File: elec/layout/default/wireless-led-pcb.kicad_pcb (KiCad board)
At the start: 4 copper layers, 154 x 30 mm, 47 parts

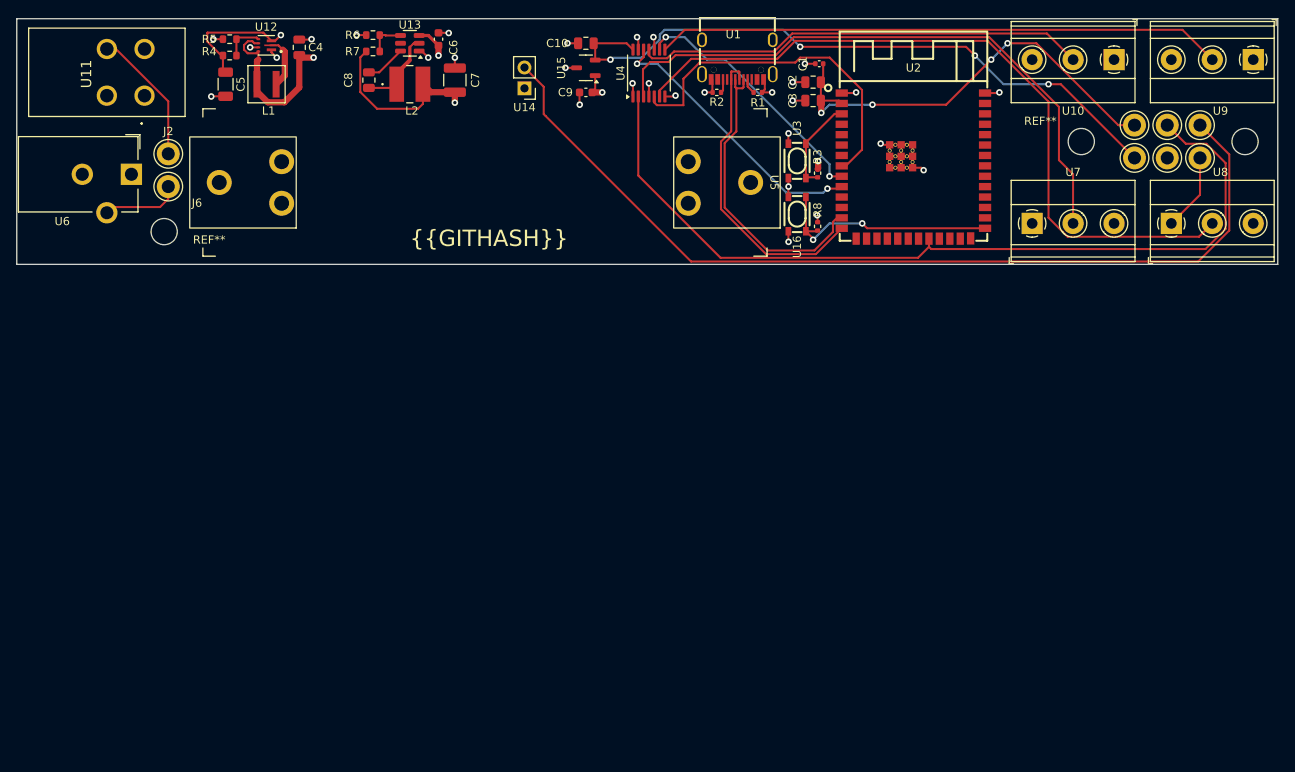
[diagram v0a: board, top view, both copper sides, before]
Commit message: totally new layout, much smaller, tons of pours.
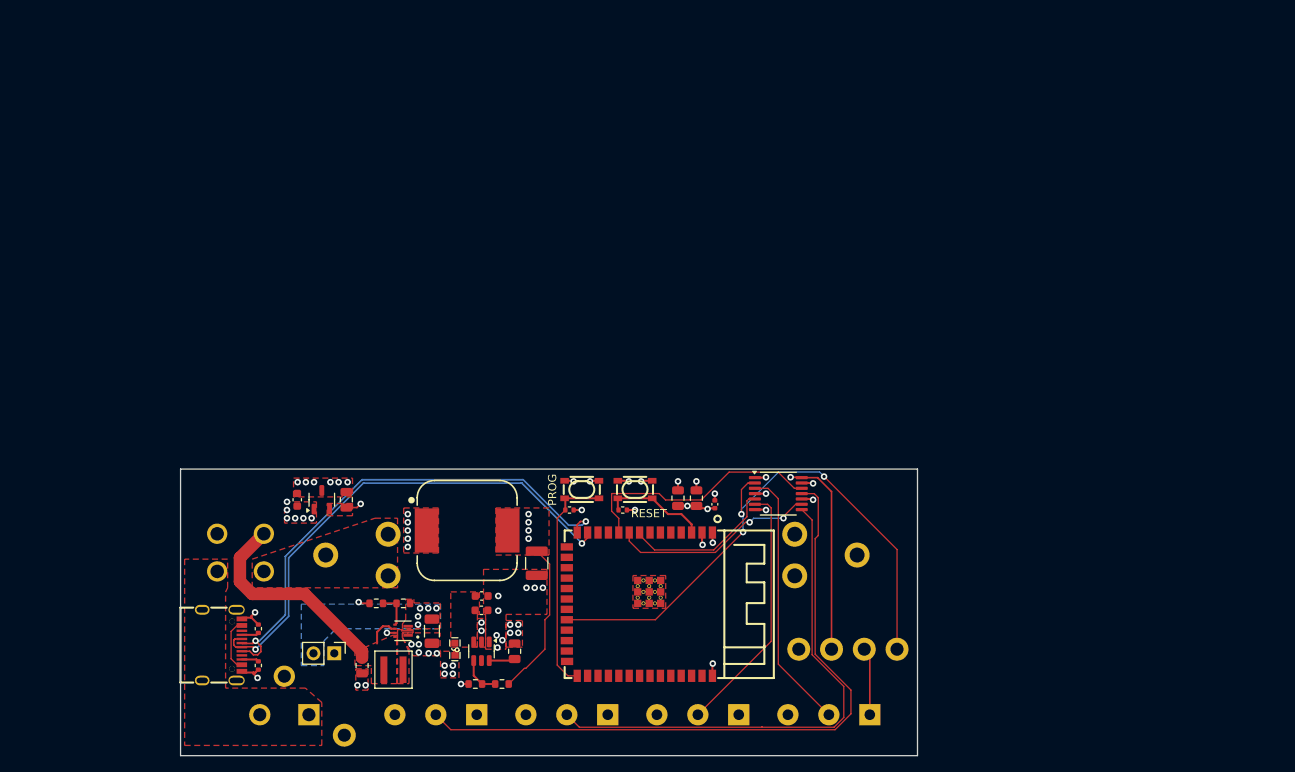
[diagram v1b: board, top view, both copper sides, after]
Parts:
- removed the J2 at (48.5, 86.5)
- removed J7, J8: , TestPoint:TestPoint_Keystone_5005-5009_Compact
- removed REF** (x3): MountingHole_3.2mm_M3, MountingHole:MountingHole_3.2mm_M3
- added C7: 50V 100nF X7R ±10% 0603 Multilayer Ceramic Capacitors MLCC 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, lib:C0603, F.Cu at (86.8, 140.5)
- added U14: , lib:F0603, F.Cu at (83.5, 147.0)
- C6: value 10V 3.3uF X5R ±10% 0603 Multilayer Ceramic Capacitors MLCC - SMD/SMT ROHS -> 25V 3.3uF X5R ±10% 0603 Multilayer Ceramic Capacitors MLCC - SMD/SMT ROHS
- J1, U10, U11, U5, U6, U7, U8, U9: moved to B.Cu
- J2: renamed from J3; moved to B.Cu
- J3: renamed from J4; moved to B.Cu
- J4: renamed from J5; moved to B.Cu
- J5: renamed from J6; moved to B.Cu
- L2: value 6.8uH +/- 20% -> 10uH +/- 20%; footprint lib:IND_8357068_WRE -> lib:WE-PD_1260
- R4: value 100mW Thick Film Resistors 150V ±100ppm/℃ ±1% 732kΩ 0603 Chip Resistor - Surface Mount ROHS -> 100mW Thick Film Resistors 75V ±100ppm/℃ ±1% 732kΩ 0603 Chip Resistor - Surface Mount ROHS
- moved J1 122.8 mm to (70.0, 157.5), turned to 180 degrees
- moved U9 112.3 mm to (102.2, 155.0)
- moved U10 111.6 mm to (86.2, 155.0)
- moved J5 102.1 mm to (133.5, 147.0), turned to 180 degrees
- moved U1 95.3 mm to (55.1, 146.5), turned to -90 degrees
- moved R2 89.6 mm to (59.5, 149.0), turned to -90 degrees
- moved R1 89.5 mm to (59.5, 144.5), turned to 90 degrees
- moved J2 80.6 mm to (125.5, 147.0), turned to 180 degrees
- moved R6 80.2 mm to (86.0, 151.2)
- moved U8 79.9 mm to (118.2, 155.0), turned to 180 degrees
- moved R7 78.8 mm to (89.2, 151.2), turned to 180 degrees
- moved C4 75.9 mm to (72.2, 149.0), turned to -90 degrees
- moved U13 74.8 mm to (86.8, 147.2), turned to -90 degrees
- moved J3 73.9 mm to (129.5, 147.0), turned to 180 degrees
- moved U12 73.4 mm to (77.2, 144.8)
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- renumbered C9 to C10, C10 to C11, C7 to C8, C8 to C9, U14 to U15, U15 to U16, U16 to U17
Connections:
- net barrel_jack-vcc renamed VJACK
- net battery_connector-vcc renamed VBAT
- net boost_3v7_to_5v.ic-fb renamed FB_BOOST
- net boost_3v7_to_5v.ic-sw renamed SW_BOOST
- net buck_wide_to_3v3.ic-fb renamed FB_BUCK
- net buck_wide_to_3v3.ic-sw renamed SW_BUCK
- net dm renamed D_N
- net dp renamed D_P
- net io15 renamed LED2_LV
- net io16 renamed LED3_LV
- net io17 renamed LED4_LV
- net mcu.ic-vcc renamed BOOT
- net out1 renamed LED1
- net out2 renamed LED2
- net out3 renamed LED3
- net out4 renamed LED4
- net pole2_b renamed VBAT_SW
- net usb_connetor-gnd renamed GND
- net usb_connetor-vcc renamed vcc
- C1 pad 1: mcu.ic-vcc-1 -> 3V3
- C10 pad 1: led_strip_connector_1-vcc -> VSYS
- C11 pad 1: level_shifter.ic-vcc -> V5_LDO
- C2 pad 1: mcu.ic-vcc-1 -> 3V3
- C3 pad 1: mcu.ic-vcc-1 -> 3V3
- C5 pad 1: boost_3v7_to_5v-vcc -> 5V
- C6 pad 1: led_strip_connector_1-vcc -> VIN_BUCK
- C8 pad 1: mcu.ic-vcc-1 -> 3V3
- J2 pad 1: boost_3v7_to_5v-vcc -> 3V3
- J3 pad 1: mcu.ic-vcc-1 -> V5_LDO
- J4 pad 1: level_shifter.ic-vcc -> LED1_LV
- J5 pad 1: detect -> VSYS
- L2 pad 2: mcu.ic-vcc-1 -> 3V3
- R3 pad 1: mcu.ic-vcc-1 -> 3V3
- R4 pad 1: boost_3v7_to_5v-vcc -> 5V
- R7 pad 1: mcu.ic-vcc-1 -> 3V3
- R8 pad 1: mcu.ic-vcc-1 -> 3V3
- U10 pad 1: led_strip_connector_1-vcc -> VSYS
- U11 pad 1: led_strip_connector_1-vcc -> VSYS
- U12 pad 3: boost_3v7_to_5v-vcc -> 5V
- U13 pad 3: led_strip_connector_1-vcc -> VIN_BUCK
- U15 pad 1: led_strip_connector_1-vcc -> VSYS
- U15 pad 2: boost_3v7_to_5v-vcc -> 5V
- U16 pad 1: led_strip_connector_1-vcc -> VSYS
- U16 pad 2: level_shifter.ic-vcc -> V5_LDO
- U2 pad 2: mcu.ic-vcc-1 -> 3V3
- U2 pad 22: tp -> LED1_LV
- U4 pad 14: level_shifter.ic-vcc -> V5_LDO
- U4 pad 2: tp -> LED1_LV
- U7 pad 1: led_strip_connector_1-vcc -> VSYS
- U8 pad 1: led_strip_connector_1-vcc -> VSYS
- U9 pad 1: led_strip_connector_1-vcc -> VSYS
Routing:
- net led_strip_connector_1-vcc: track 198.9 -> 0.00 mm, vias 2 -> 0
- net boost_3v7_to_5v-vcc: track 163.0 -> 0.00 mm, vias 1 -> 0
- net mcu.ic-vcc-1: track 136.6 -> 0.00 mm, vias 7 -> 0
- net VBAT: track 110.9 -> 0.00 mm
- net tp: track 105.3 -> 0.00 mm
- net level_shifter.ic-vcc: track 81.5 -> 0.00 mm, vias 4 -> 0
- net V5_LDO: track 0.00 -> 81.3 mm, vias 0 -> 2
- net LED1_LV: track 0.00 -> 70.8 mm, vias 0 -> 3
- net LED2: track 89.6 -> 31.1 mm
- net 3V3: track 0.00 -> 44.8 mm, vias 0 -> 9
- net LED1: track 74.2 -> 32.3 mm
- net GND: track 61.6 -> 27.3 mm, vias 29 -> 40
- net LED4: track 55.2 -> 82.9 mm
- net D_P: track 37.6 -> 63.4 mm, vias 0 -> 2
- net D_N: track 37.0 -> 61.7 mm, vias 0 -> 2
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- added copper zone on F.Cu, net 3V3
- added copper zone on In2.Cu, net 3V3
- added copper zone on B.Cu, net 5V
- added copper zone on F.Cu, net 5V
- added copper zone on F.Cu, net GND
- added copper zone on F.Cu, net SW_BOOST
- added copper zone on F.Cu, net SW_BUCK
- added copper zone on In2.Cu, net SW_BUCK
- added copper zone on F.Cu, net V5_LDO
- added copper zone on F.Cu, net VBAT
- added copper zone on F.Cu, net VBAT_SW
- added copper zone on F.Cu, net VIN_BUCK
- added copper zone on F.Cu, net VJACK
- added copper zone on F.Cu, net VSYS
- added copper zone on In2.Cu, net VSYS
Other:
- board size 154 x 30 mm -> 90 x 35 mm
- board text added: "1"
- board text added: "2"
- board text added: "3"
- board text added: "3.3V"
- board text added: "4"
- board text added: "5V"
- board text added: "5V - 24V"
- board text added: "BAT+"
- board text added: "BATT"
- board text added: "D"
- board text added: "D1"
- board text added: "G"
- board text added: "GND"
- board text added: "OFF"
- board text added: "ON"
- board text added: "P"
- board text added: "PROG"
- board text added: "RESET"
- board text added: "VSYS"
